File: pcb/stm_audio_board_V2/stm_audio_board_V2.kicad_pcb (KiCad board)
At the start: 4 copper layers, 66 x 71.1 mm, 140 parts, among them J1 Power conn, J2 STlink, J3 Audio_sig, J4 Conn_01x01_taptempo, J5 Conn_01x10_display, J6 Conn_01x03_pot_ext, J7 Conn_01x8_pots_internal, SW1 SW_SPST, U1 STM32H747IGTx, U2 OP275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

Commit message: updated pcb design
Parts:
- moved C71 3.05 mm to (238.0, 86.2), turned to 180 degrees
- moved D5 3.05 mm to (234.9, 77.7)
- moved U9 3.05 mm to (241.3, 78.8)
- moved C102 3.05 mm to (234.5, 75.6)
- moved C70 3.05 mm to (237.8, 73.6)
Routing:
- net 5V: track 88.0 -> 87.0 mm
- net AD1939_CM: track 27.8 -> 28.7 mm
- net GND: track 234.9 -> 235.5 mm, vias 115 -> 119

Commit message: Update stm_audio_board_V2-B_Cu.gbr, stm_audio_board_V2-B_Mask.gbr, and 29 more files...
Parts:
- added C36: 100nF, Capacitor_SMD:C_0603_1608Metric_Pad1.08x0.95mm_HandSolder, B.Cu at (212.4, 86.0)
- moved C80 2.79 mm to (218.9, 92.7), turned to 0 degrees
- moved C16 1.61 mm to (206.6, 74.6)
- moved C104 1.02 mm to (185.4, 89.3)
- moved C9 0.51 mm to (212.8, 79.2), turned to 180 degrees
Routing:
- net GND: track 235.5 -> 204.4 mm, vias 119 -> 121
- net +3.3V: track 333.2 -> 317.7 mm, vias 15 -> 13
- net AD1939_FILTR: track 11.0 -> 9.02 mm
- net DISPLAY_DC: track 18.3 -> 19.8 mm
- net /MCU/NRST: track 26.4 -> 27.7 mm
- net TOUCH_CS: track 11.5 -> 12.6 mm
- net Net-(C22-Pad2): track 10.6 -> 9.65 mm
- net ADC1N: track 7.10 -> 6.19 mm
- net Net-(U4A--): track 15.5 -> 14.6 mm
- net POT5: track 17.1 -> 17.9 mm
- net Net-(U4B--): track 12.1 -> 11.3 mm
- net 5V: track 87.0 -> 87.8 mm
- net TOUCH_IRQ: track 13.0 -> 13.8 mm
- net ADC1P: track 6.69 -> 5.97 mm
- net DISPLAY_MISO: track 22.1 -> 22.9 mm
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- added copper zone on In2.Cu, net GND

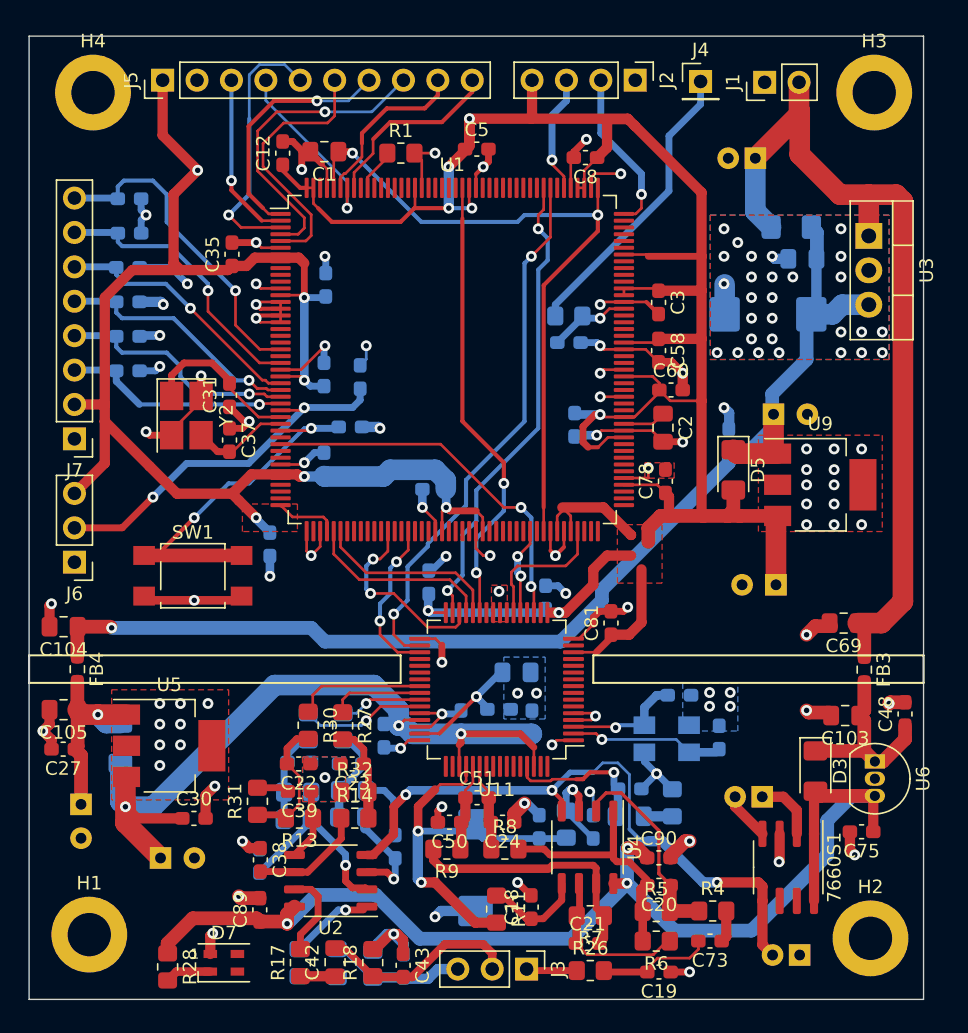
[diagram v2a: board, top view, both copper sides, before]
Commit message: silkscreen updated
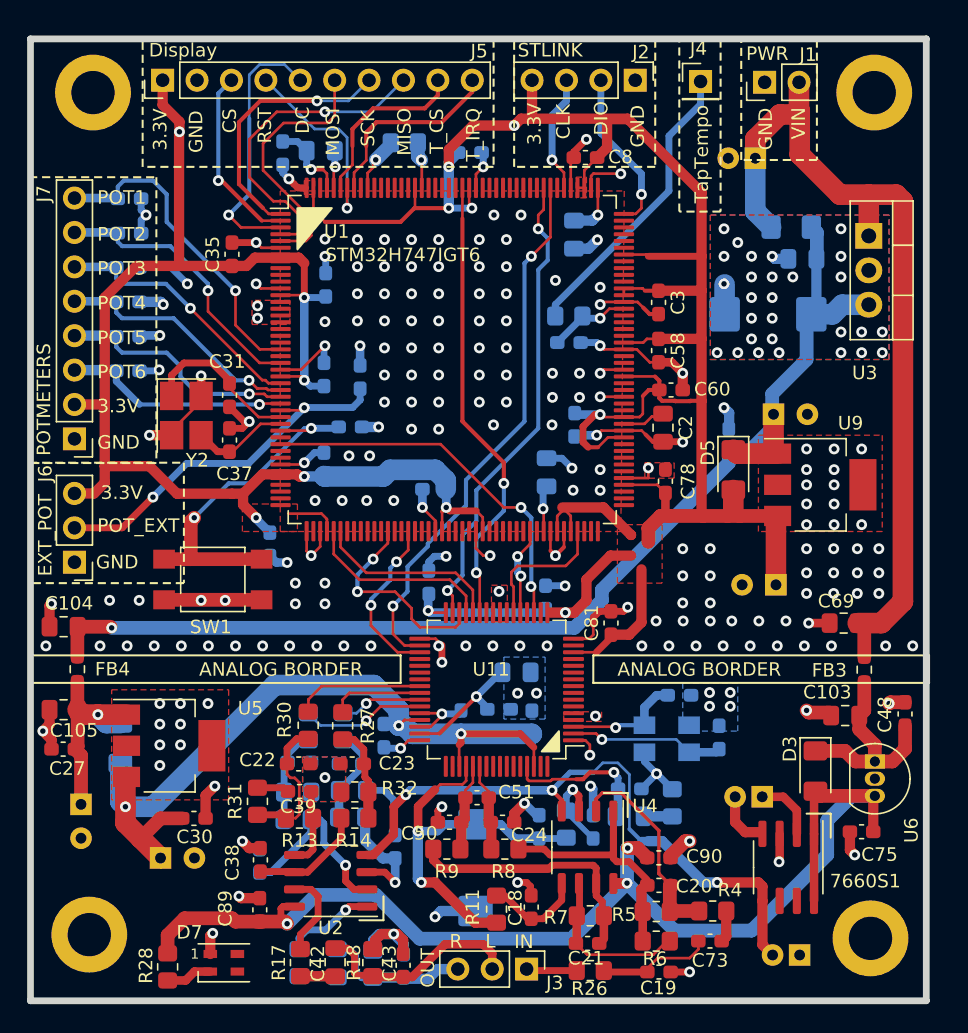
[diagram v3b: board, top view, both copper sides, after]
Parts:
- added C49: 2.2uF, Capacitor_SMD:C_0805_2012Metric_Pad1.18x1.45mm_HandSolder, B.Cu at (223.1, 60.4)
- added C52: 2.2uF, Capacitor_SMD:C_0805_2012Metric_Pad1.18x1.45mm_HandSolder, B.Cu at (204.4, 54.2)
- C1, C12, C5, R1: moved to B.Cu
- C42, C46: value 47uF -> 2u2
- moved C1 28.8 mm to (221.1, 77.9), turned to 90 degrees
- moved SW1 1.50 mm to (196.4, 85.8)
- moved R1 0.80 mm to (210.6, 53.6)
- moved C5 0.57 mm to (215.4, 54.3)
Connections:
- U1 pad 133: Net-(C1-Pad1) -> Net-(C49-Pad1)
- U1 pad 172: Net-(C1-Pad1) -> Net-(C52-Pad1)
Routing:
- net Net-(C1-Pad1): track 50.8 -> 3.44 mm, vias 2 -> 1
- net GND: track 204.4 -> 194.7 mm, vias 121 -> 243
- net Net-(C49-Pad1): track 0.00 -> 3.94 mm, vias 0 -> 1
- net Net-(C52-Pad1): track 0.00 -> 2.86 mm, vias 0 -> 1
- net /MCU/NRST: track 27.7 -> 26.0 mm
- net Net-(D3-K): track 14.0 -> 15.5 mm
- net +9V: track 86.9 -> 88.2 mm
- net GUITAR_OUT_R: track 9.44 -> 10.7 mm
- net Net-(U1-BOOT0): track 2.84 -> 4.04 mm, vias 0 -> 1
- net AD1939_SPI3_MOSI: track 14.2 -> 15.4 mm
- net DISPLAY_SCK: track 18.3 -> 19.4 mm
- net DISPLAY_RST: track 13.4 -> 14.5 mm
- net Net-(U2A-+): track 7.72 -> 8.68 mm
- net DISPLAY_CS: track 12.7 -> 13.6 mm
- net Net-(U2A--): track 12.8 -> 13.7 mm
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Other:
- board size 66 x 71.1 mm -> 66.1 x 71 mm
- board text added: "3.3V"
- board text added: "ANALOG BORDER"
- board text added: "Auth: Papp Aron"
- board text added: "CLK"
- board text added: "CS"
- board text added: "DC"
- board text added: "DIO"
- board text added: "Date: 2023.11.02."
- board text added: "Display"
- board text added: "EXT_POT"
- board text added: "GND"
- board text added: "IN"
- board text added: "L"
- board text added: "MISO"
- board text added: "MOSI"
- board text added: "OUT"
- board text added: "POT1"
- board text added: "POT2"
- board text added: "POT3"
- board text added: "POT4"
- board text added: "POT5"
- board text added: "POT6"
- board text added: "POTMETERS"
- board text added: "POT_EXT"
- board text added: "PWR"
- board text added: "R"
- board text added: "RST"
- board text added: "SCK"
- board text added: "STLINK"
- board text added: "STM32H747IGT6"
- board text added: "STM_AUDIO_BOARD_V2"
- board text added: "T_CS"
- board text added: "T_IRQ"
- board text added: "TapTempo"
- board text added: "VIN"
- board text added: "WARNING! VIN: 12-18V min 500mA"

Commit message: Update output_not_finished.zip, stm_audio_board_V2-B_Cu.gbl, and 44 more files...
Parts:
- moved H1 0.39 mm to (187.6, 112.3)
- moved H3 0.19 mm to (245.1, 49.8)
- moved H2 0.10 mm to (245.1, 112.3)
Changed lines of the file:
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@@
     )
     (pad_to_mask_clearance 0)
+    (aux_axis_origin 182.9816 116.9416)
     (grid_origin 198.12 78.74)
     (pcbplotparams
@@
       (plot_on_all_layers_selection 0x0000000_00000000)
       (disableapertmacros false)
-      (usegerberextensions false)
-      (usegerberattributes true)
-      (usegerberadvancedattributes true)
-      (creategerberjobfile true)
+      (usegerberextensions true)
+      (usegerberattributes false)
+      (usegerberadvancedattributes false)
+      (creategerberjobfile false)
       (dashed_line_dash_ratio 12.000000)
       (dashed_line_gap_ratio 3.000000)
@@
       (psa4output false)
       (plotreference true)
-      (plotvalue true)
+      (plotvalue false)
       (plotinvisibletext false)
       (sketchpadsonfab false)
-      (subtractmaskfromsilk false)
+      (subtractmaskfromsilk true)
       (outputformat 1)
       (mirror false)
@@
   )
   (footprint "MountingHole:MountingHole_3.2mm_M3_DIN965_Pad" (layer "F.Cu")
-    (at 245.003 112.333)
+    (at 245.099 112.333)
     (descr "Mounting Hole 3.2mm, M3, DIN965")
     (tags "mounting hole 3.2mm m3 din965")
@@
   )
   (footprint "MountingHole:MountingHole_3.2mm_M3_DIN965_Pad" (layer "F.Cu")
-    (at 245.278 49.887)
+    (at 245.099 49.833)
     (descr "Mounting Hole 3.2mm, M3, DIN965")
     (tags "mounting hole 3.2mm m3 din965")
@@
   )
   (footprint "MountingHole:MountingHole_3.2mm_M3_DIN965_Pad" (layer "F.Cu")
-    (at 187.324 112.058)
+    (at 187.599 112.333)
     (descr "Mounting Hole 3.2mm, M3, DIN965")
     (tags "mounting hole 3.2mm m3 din965")
@@
     (fp_line (start 1 0.625) (end 1 -0.625)
       (stroke (width 0.1) (type solid)) (layer "B.Fab"))
-    (pad "1" smd roundrect (at -1.0375 0 270) (size 1.175 1.45) (layers "B.Cu" "B.Paste" "B.Mask") (roundrect_rratio 0.212766)
+    (pad "1" smd roundrect (at -1.0375 0 270) (size 1.175 1.45) (layers "B.Cu" "B.Paste" "B.Mask") (roundrect_rratio 0.2127659574)
       (net 202 "Net-(C49-Pad1)") (pintype "passive"))
-    (pad "2" smd roundrect (at 1.0375 0 270) (size 1.175 1.45) (layers "B.Cu" "B.Paste" "B.Mask") (roundrect_rratio 0.212766)
+    (pad "2" smd roundrect (at 1.0375 0 270) (size 1.175 1.45) (layers "B.Cu" "B.Paste" "B.Mask") (roundrect_rratio 0.2127659574)
       (net 1 "GND") (pintype "passive"))
     (model "${KICAD6_3DMODEL_DIR}/Capacitor_SMD.3dshapes/C_0805_2012Metric.wrl"
@@
     (fp_line (start 1 0.625) (end 1 -0.625)
       (stroke (width 0.1) (type solid)) (layer "B.Fab"))
-    (pad "1" smd roundrect (at -1.0375 0 180) (size 1.175 1.45) (layers "B.Cu" "B.Paste" "B.Mask") (roundrect_rratio 0.212766)
+    (pad "1" smd roundrect (at -1.0375 0 180) (size 1.175 1.45) (layers "B.Cu" "B.Paste" "B.Mask") (roundrect_rratio 0.2127659574)
       (net 203 "Net-(C52-Pad1)") (pintype "passive"))
-    (pad "2" smd roundrect (at 1.0375 0 180) (size 1.175 1.45) (layers "B.Cu" "B.Paste" "B.Mask") (roundrect_rratio 0.212766)
+    (pad "2" smd roundrect (at 1.0375 0 180) (size 1.175 1.45) (layers "B.Cu" "B.Paste" "B.Mask") (roundrect_rratio 0.2127659574)
       (net 1 "GND") (pintype "passive"))
     (model "${KICAD6_3DMODEL_DIR}/Capacitor_SMD.3dshapes/C_0805_2012Metric.wrl"
@@
     (effects (font (size 1 1) (thickness 0.15)) (justify left bottom mirror))
   )
-  (gr_text "ANALOG BORDER" (at 226.314 93.0656) (layer "F.SilkS" knockout)
+  (gr_text "ANALOG BORDER" (at 226.822 93.0656) (layer "F.SilkS" knockout)
     (effects (font (size 1 1) (thickness 0.15)) (justify left bottom))
   )

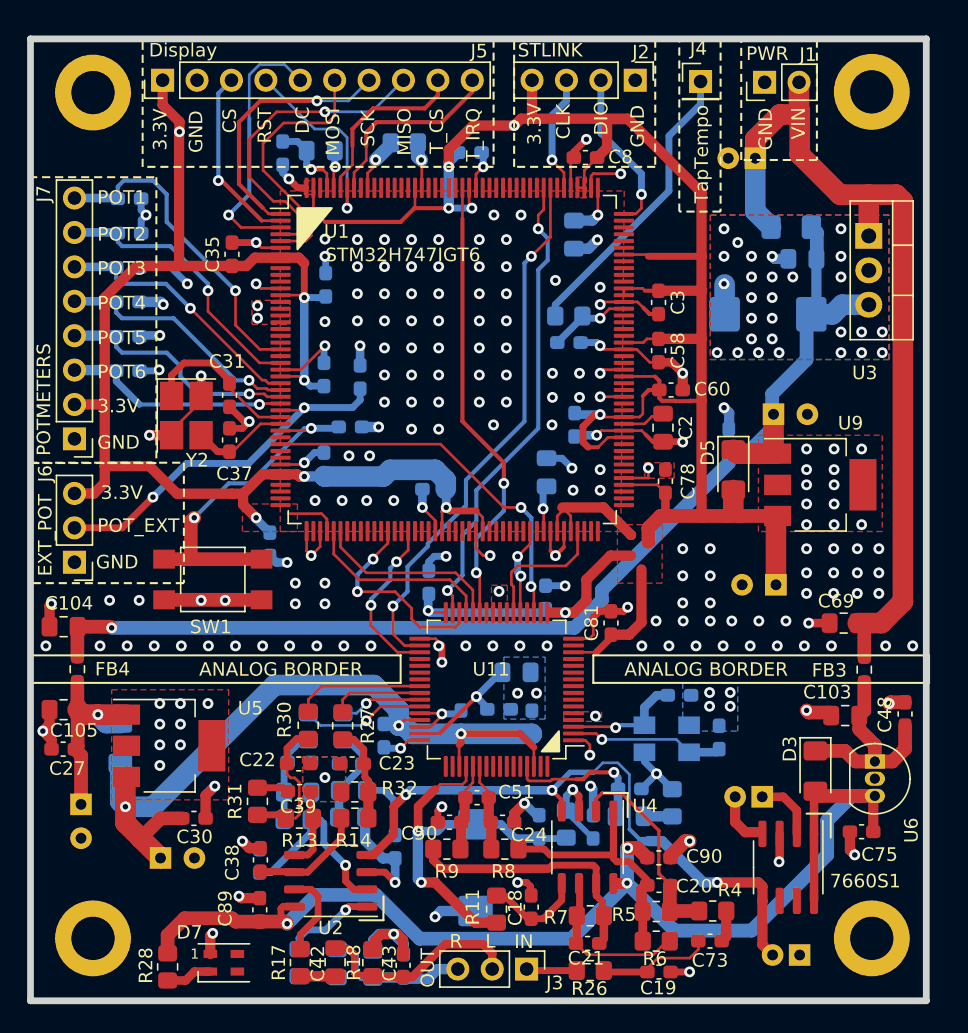
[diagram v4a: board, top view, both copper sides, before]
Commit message: added vias and overall fixes around pcb
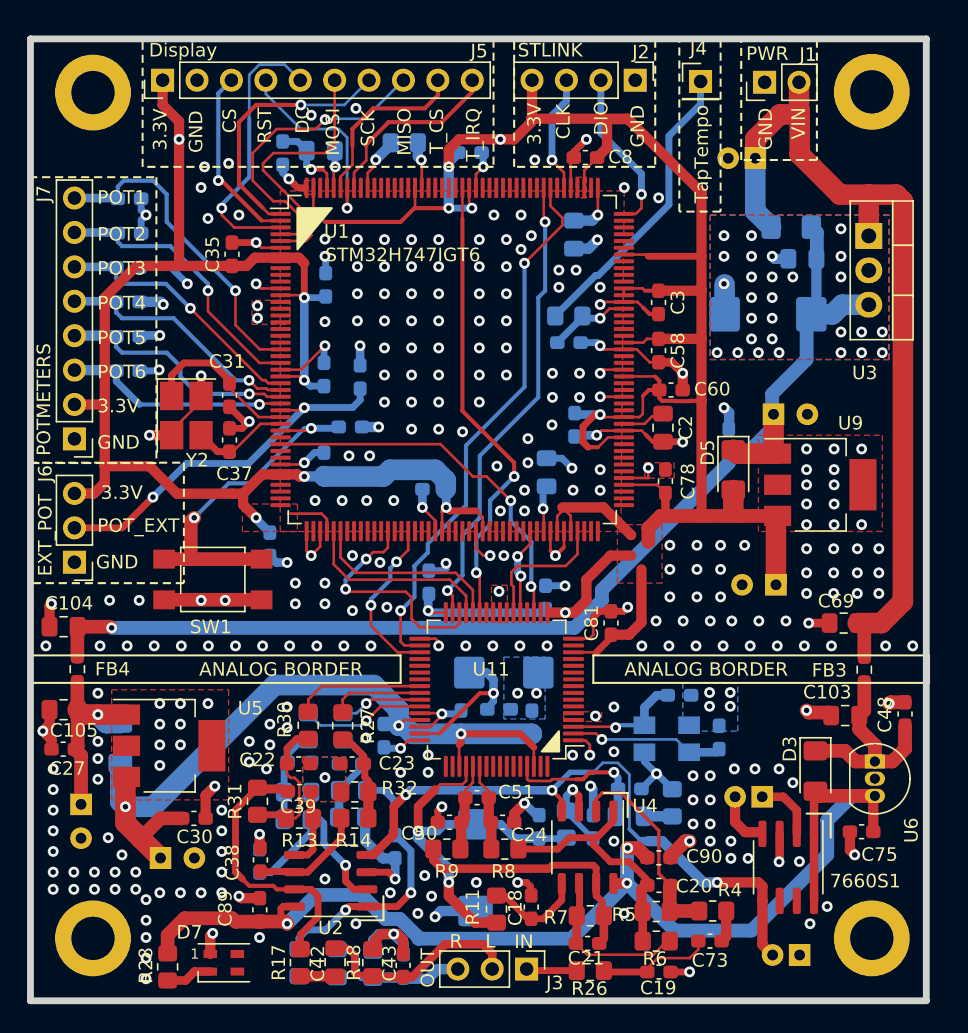
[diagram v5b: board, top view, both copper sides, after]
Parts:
- C80: footprint Capacitor_SMD:C_0805_2012Metric_Pad1.18x1.45mm_HandSolder -> Capacitor_Tantalum_SMD:CP_EIA-6032-28_Kemet-C_Pad2.25x2.35mm_HandSolder
- moved C80 0.94 mm to (217.9, 92.7)
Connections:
- R17 pad 2: Net-(R17-Pad2) -> Net-(C39-Pad2)
- R23 pad 2: Net-(R23-Pad2) -> Net-(C44-Pad2)
- U2 pad 1: Net-(R23-Pad2) -> Net-(C44-Pad2)
- U2 pad 7: Net-(R17-Pad2) -> Net-(C39-Pad2)
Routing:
- net Net-(C39-Pad2): track 1.98 -> 22.3 mm
- net Net-(C44-Pad2): track 4.82 -> 20.0 mm, vias 0 -> 2
- net Net-(R23-Pad2): track 6.80 -> 0.00 mm, vias 1 -> 0
- net Net-(R17-Pad2): track 6.39 -> 0.00 mm
- net GND: track 194.7 -> 188.8 mm, vias 243 -> 344
- net AD1939_SPI3_MOSI: track 15.4 -> 17.4 mm
- net AD1939_FILTR: track 9.02 -> 11.0 mm
- net Net-(C20-Pad2): track 20.5 -> 18.7 mm
- net +3.3V: track 317.8 -> 316.3 mm
- net DISPLAY_MISO: track 23.5 -> 22.5 mm
- net DISPLAY_DC: track 19.8 -> 20.5 mm
- net AD1939_I2S1_SDI: track 33.6 -> 34.2 mm
- net AD1939_CM: track 29.4 -> 28.8 mm
- net DISPLAY_RST: track 14.5 -> 15.1 mm
- net TOUCH_IRQ: track 14.4 -> 13.9 mm

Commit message: stm_audio_board_V2 is finished, sent to jlcPCB for production
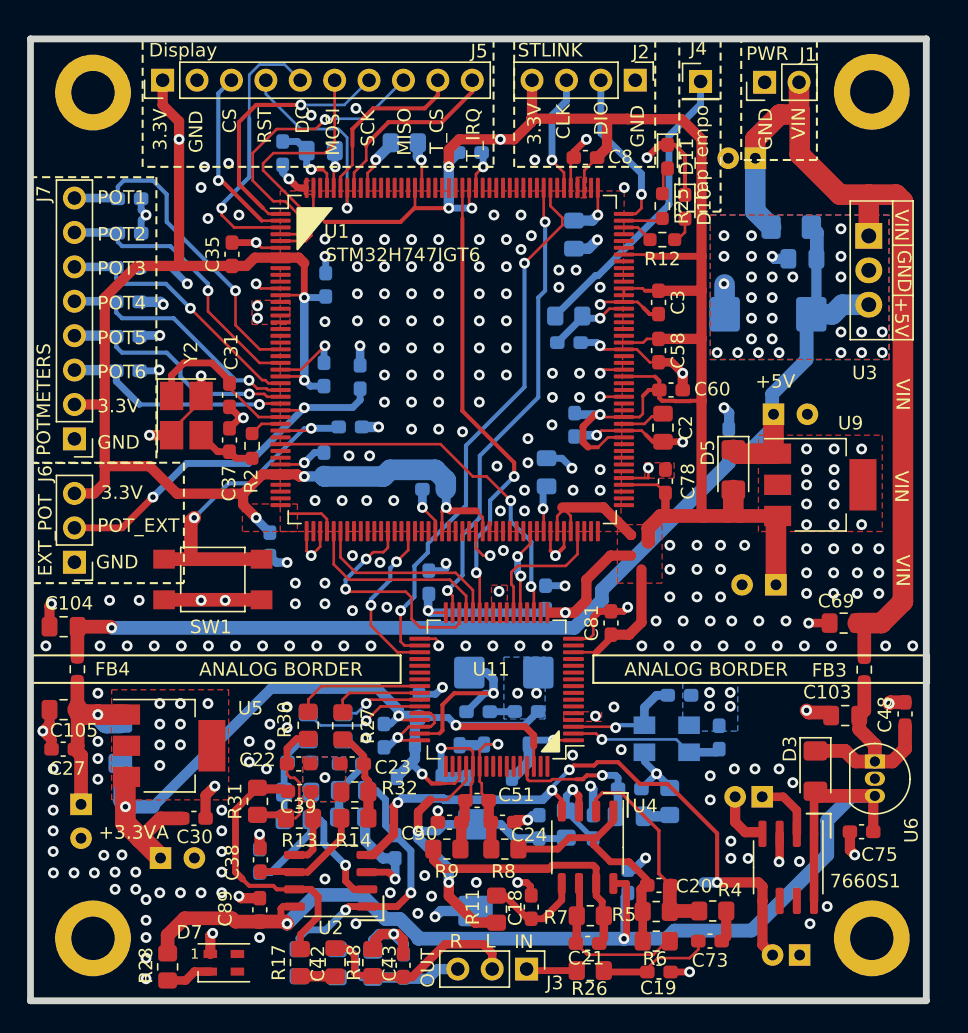
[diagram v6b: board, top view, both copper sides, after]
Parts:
- added D10: LED, LED_SMD:LED_0603_1608Metric_Pad1.05x0.95mm_HandSolder, F.Cu at (231.3, 58.3)
- added D11: LED, LED_SMD:LED_0603_1608Metric_Pad1.05x0.95mm_HandSolder, F.Cu at (230.0, 54.6)
- added D4: BAT42W-V, Diode_SMD:D_SOD-123, B.Cu at (216.9, 100.5)
- added D6: BAT42W-V, Diode_SMD:D_SOD-123, B.Cu at (211.7, 100.4)
- added D8: BAT42W-V, Diode_SMD:D_SOD-123, B.Cu at (218.1, 98.0)
- added D9: BAT42W-V, Diode_SMD:D_SOD-123, B.Cu at (213.0, 98.1)
- added R12: 1k NC, Resistor_SMD:R_0603_1608Metric_Pad0.98x0.95mm_HandSolder, F.Cu at (229.6, 60.7)
- added R2: 100R NC, Resistor_SMD:R_0603_1608Metric_Pad0.98x0.95mm_HandSolder, F.Cu at (199.3, 76.0)
- added R25: 1k, Resistor_SMD:R_0603_1608Metric_Pad0.98x0.95mm_HandSolder, F.Cu at (229.6, 58.3)
- C26: value 100uF tantal -> 47uF tantal
- C90: moved to B.Cu
- moved C32 3.32 mm to (211.7, 95.2)
- moved C90 2.87 mm to (227.1, 108.1), turned to 90 degrees
- moved C79 1.55 mm to (216.0, 95.6)
- moved C34 0.89 mm to (219.6, 95.6), turned to 180 degrees
- moved R10 0.22 mm to (230.2, 102.2)
- moved C51 0.20 mm to (216.0, 102.2)
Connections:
- C37 pad 2: OSC1 -> Net-(C37-Pad2)
- U1 pad 130: unconnected-(U1-PA11-Pad130) -> LED1
- U1 pad 131: unconnected-(U1-PA12-Pad131) -> LED2
- U1 pad 174: unconnected-(U1-PDR_ON-Pad174) -> GND
- Y2 pad 3: OSC1 -> Net-(C37-Pad2)
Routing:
- net GND: track 188.8 -> 199.6 mm, vias 344 -> 331
- net +3.3VA: track 63.7 -> 73.5 mm, vias 3 -> 4
- net ADC1P: track 6.40 -> 14.4 mm, vias 0 -> 1
- net ADC1N: track 6.19 -> 11.8 mm, vias 0 -> 1
- net Net-(C37-Pad2): track 0.00 -> 4.47 mm
- net OSC1: track 6.87 -> 2.40 mm
- net LED2: track 0.00 -> 2.91 mm
- net AD1939_FILTR: track 11.0 -> 13.4 mm
- net +3.3V: track 316.3 -> 318.6 mm
- net LED1: track 0.00 -> 2.30 mm
- net Net-(D11-A): track 0.00 -> 2.01 mm
- net Net-(D10-A): track 0.00 -> 1.99 mm
- net -9V: track 46.6 -> 47.6 mm, vias 3 -> 4
- net +9V: track 88.2 -> 88.4 mm, vias 3 -> 2
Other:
- board text added: "+3.3VA"
- board text added: "+5V"
- board text added: "JLCJLCJLCJLC"
